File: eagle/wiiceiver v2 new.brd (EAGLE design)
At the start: 40 x 58.5 mm, 21 parts, among them IC1 ATmega328P

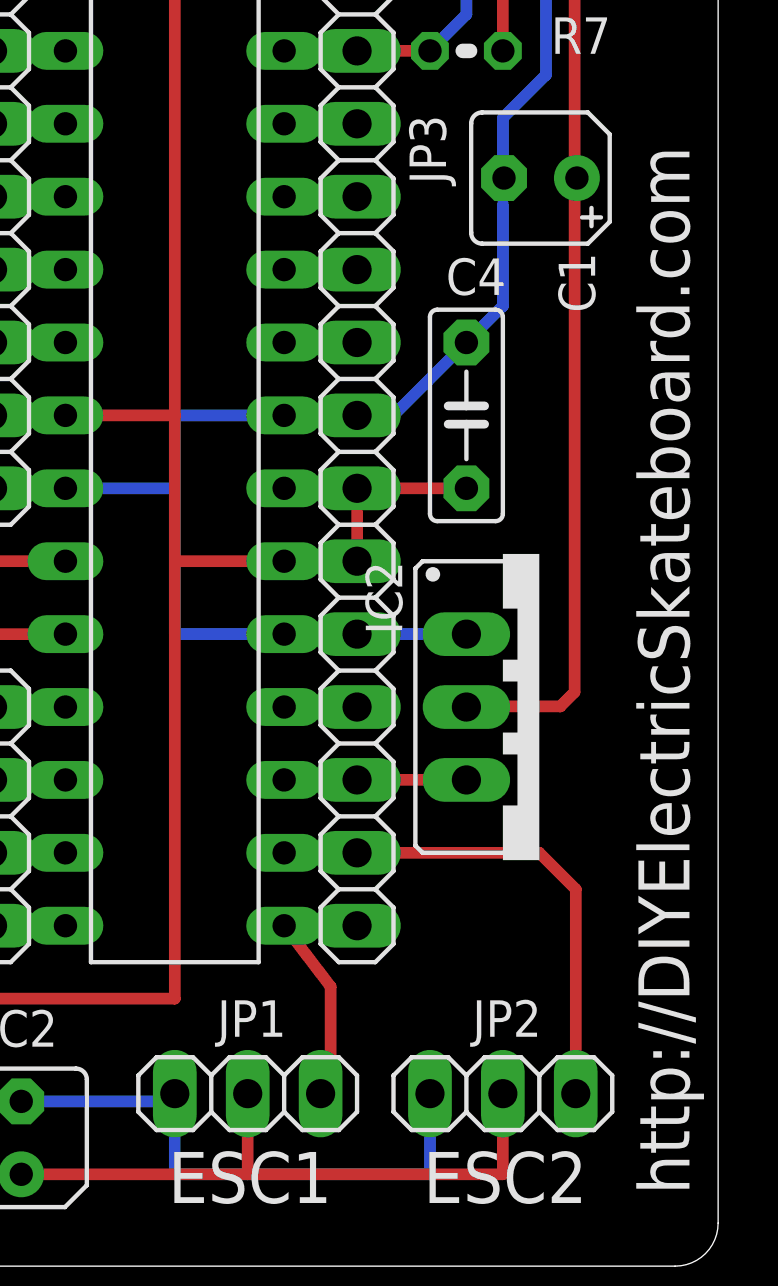
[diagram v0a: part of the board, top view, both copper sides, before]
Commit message: minor changes due to voilations in ERC
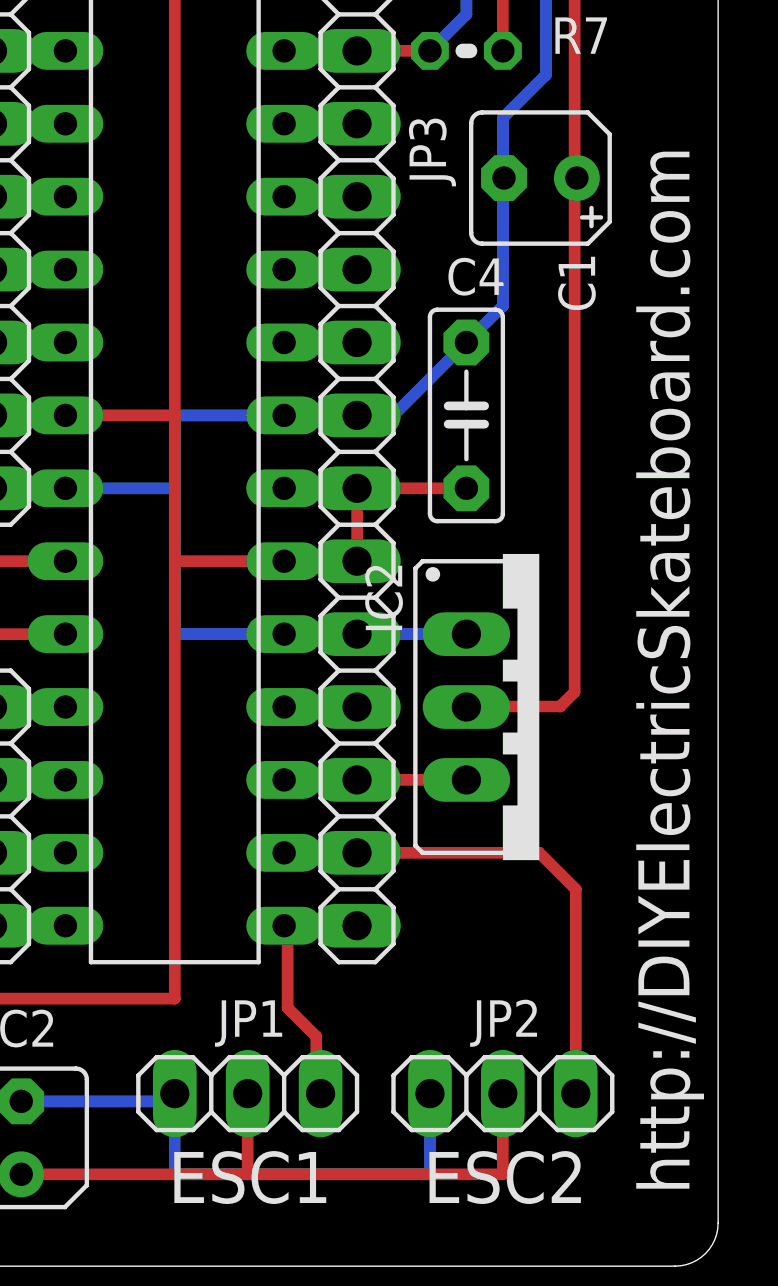
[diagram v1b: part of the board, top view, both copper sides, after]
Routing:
- net D10: track 15.3 -> 17.8 mm
- net D9: track 10.2 -> 8.92 mm
- net GND: track 140.9 -> 141.8 mm
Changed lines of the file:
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@@
 <?xml version="1.0" encoding="utf-8"?>
 <!DOCTYPE eagle SYSTEM "eagle.dtd">
-<eagle version="7.1.0">
+<eagle version="7.4.0">
 <drawing>
 <settings>
@@
 <layer number="42" name="bRestrict" color="1" fill="10" visible="yes" active="yes"/>
 <layer number="43" name="vRestrict" color="2" fill="10" visible="yes" active="yes"/>
-<layer number="44" name="Drills" color="7" fill="1" visible="no" active="yes"/>
+<layer number="44" name="Drills" color="7" fill="1" visible="yes" active="yes"/>
 <layer number="45" name="Holes" color="7" fill="1" visible="yes" active="yes"/>
 <layer number="46" name="Milling" color="3" fill="1" visible="yes" active="yes"/>
@@
 <contactref element="JP3" pad="14"/>
 <wire x1="55.88" y1="22.86" x2="58.42" y2="22.86" width="0.4064" layer="1"/>
-<wire x1="57.15" y1="17.01" x2="57.5" y2="16.51" width="0.4064" layer="16"/>
-<wire x1="57.5" y1="19" x2="56" y2="20.5" width="0" layer="19" extent="1-16"/>
-<wire x1="56" y1="20.5" x2="56" y2="22.74" width="0" layer="19" extent="1-16"/>
 <wire x1="56" y1="22.74" x2="55.88" y2="22.86" width="0.4064" layer="1"/>
-<wire x1="57.5" y1="16.51" x2="57.5" y2="16.51" width="0" layer="19" extent="1-16"/>
-<wire x1="57.5" y1="16.51" x2="57.5" y2="20.74" width="0.4064" layer="1"/>
-<wire x1="57.5" y1="20.74" x2="55.88" y2="22.86" width="0.4064" layer="1"/>
+<wire x1="56" y1="22.74" x2="56" y2="20" width="0.4064" layer="1"/>
+<wire x1="56" y1="20" x2="57" y2="19" width="0.4064" layer="1"/>
+<wire x1="57" y1="19" x2="57" y2="17.16" width="0.4064" layer="1"/>
+<wire x1="57" y1="17.16" x2="57.15" y2="17.01" width="0.4064" layer="1"/>
 </signal>
 <signal name="D8">
@@
 <wire x1="66" y1="57" x2="64.27" y2="58.73" width="0.4064" layer="1"/>
 <wire x1="64.27" y1="58.73" x2="64.23" y2="58.73" width="0.4064" layer="1"/>
-<wire x1="67.31" y1="30.48" x2="66.08" y2="48.91" width="0" layer="19" extent="1-1"/>
 <wire x1="62.23" y1="30.48" x2="62.25" y2="30.5" width="0.4064" layer="1"/>
 <wire x1="62.25" y1="30.5" x2="65.5" y2="30.5" width="0.4064" layer="1"/>
 <wire x1="65.5" y1="30.5" x2="66" y2="31" width="0.4064" layer="1"/>
 <wire x1="66" y1="31" x2="66" y2="48.5" width="0.4064" layer="1"/>
-<wire x1="66" y1="48.5" x2="66.08" y2="48.91" width="0" layer="19" extent="1-16"/>
+<wire x1="66" y1="48.5" x2="66.08" y2="48.5" width="0.4064" layer="1"/>
+<wire x1="66.08" y1="48.5" x2="66.08" y2="48.91" width="0.4064" layer="1"/>
+<wire x1="67.31" y1="30.48" x2="66.08" y2="48.91" width="0" layer="19" extent="1-1"/>
 </signal>
 <signal name="D5">
@@
 <wire x1="36.83" y1="16.74" x2="35.56" y2="18.01" width="0.4064" layer="16"/>
 <wire x1="35.56" y1="18.01" x2="35.56" y2="21.59" width="0.4064" layer="16"/>
-<wire x1="63.54" y1="48.91" x2="63.5" y2="48.91" width="0.4064" layer="16"/>
 <wire x1="63.5" y1="48.91" x2="63.5" y2="51" width="0.4064" layer="16"/>
 <wire x1="66" y1="58.5" x2="65" y2="59.5" width="0" layer="19" extent="1-16"/>
@@
 <wire x1="63.77" y1="60.73" x2="55.88" y2="60.73" width="0.4064" layer="16"/>
 <wire x1="62.23" y1="43.18" x2="63.5" y2="44.45" width="0.4064" layer="16"/>
-<wire x1="63.5" y1="44.45" x2="63.5" y2="48" width="0.4064" layer="16"/>
+<wire x1="63.5" y1="44.45" x2="63.5" y2="48.91" width="0.4064" layer="16"/>
 <wire x1="63.5" y1="51" x2="65" y2="52.5" width="0.4064" layer="16"/>
 <wire x1="65" y1="52.5" x2="65" y2="59.5" width="0.4064" layer="16"/>
-<wire x1="63.5" y1="48" x2="63.54" y2="48.91" width="0" layer="19" extent="16-16"/>
+<wire x1="63.54" y1="48.91" x2="63.5" y2="48.91" width="0.4064" layer="16"/>
 </signal>
 <signal name="VIN">
@@
 <contactref element="IC1" pad="16"/>
 <contactref element="JP3" pad="13"/>
-<wire x1="55.88" y1="25.4" x2="58.42" y2="25.4" width="0" layer="19" extent="1-1"/>
 <wire x1="58.42" y1="25.4" x2="64.77" y2="25.4" width="0.4064" layer="1"/>
 <wire x1="64.77" y1="25.4" x2="66.04" y2="24.13" width="0.4064" layer="1"/>
 <wire x1="66.04" y1="24.13" x2="66.04" y2="17.01" width="0.4064" layer="1"/>
+<wire x1="55.88" y1="25.4" x2="58.42" y2="25.4" width="0.4064" layer="1"/>
 </signal>
 <signal name="A3">
